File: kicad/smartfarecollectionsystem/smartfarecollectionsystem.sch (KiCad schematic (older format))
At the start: 3 parts

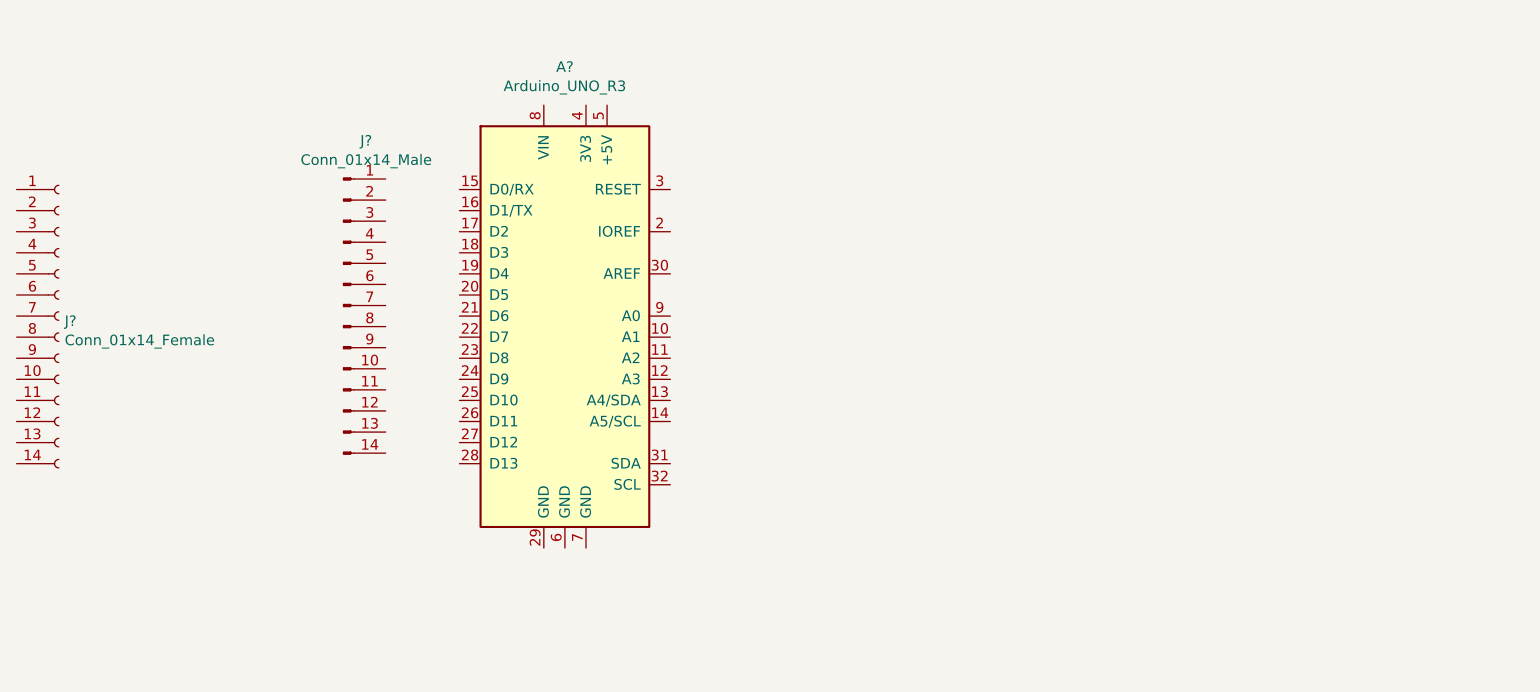
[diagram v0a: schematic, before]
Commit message: ip address changed and PCB layout made
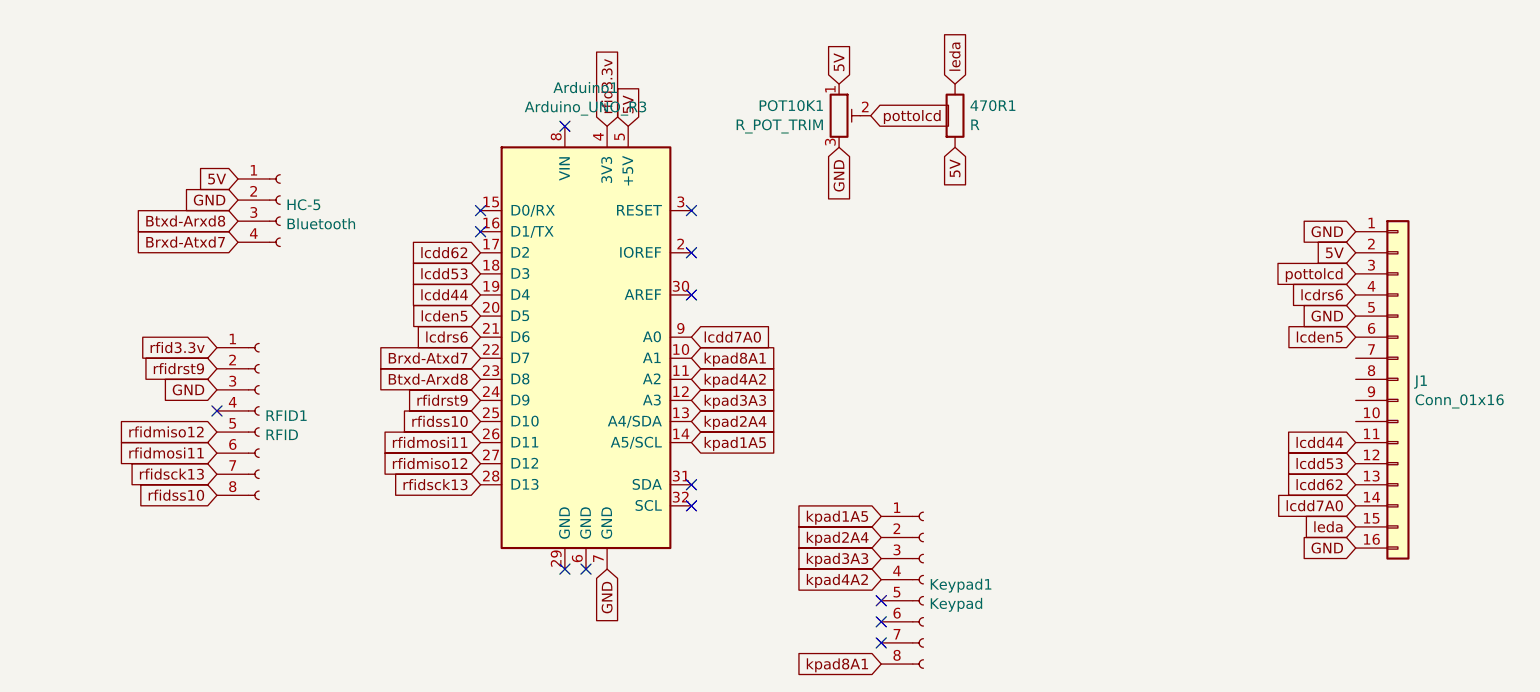
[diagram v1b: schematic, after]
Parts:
- removed J?: Conn_01x14_Female, symbol Connector:Conn_01x14_Female
- removed J?: Conn_01x14_Male, symbol Connector:Conn_01x14_Male
- added 470R1: R, Resistor_THT:R_Axial_DIN0207_L6.3mm_D2.5mm_P7.62mm_Horizontal, symbol Device:R
- added HC-5: Bluetooth, Connector_PinHeader_2.54mm:PinHeader_1x04_P2.54mm_Vertical, symbol Connector:Conn_01x04_Female
- added J1: Conn_01x16, Display:WC1602A, symbol Connector_Generic:Conn_01x16
- added Keypad1: Keypad, Connector_PinHeader_2.54mm:PinHeader_1x08_P2.54mm_Vertical, symbol Connector:Conn_01x08_Female
- added POT10K1: R_POT_TRIM, Potentiometer_THT:Potentiometer_Piher_PT-10-V05_Vertical, symbol Device:R_POT_TRIM
- added RFID1: RFID, Connector_PinHeader_2.54mm:PinHeader_1x08_P2.54mm_Vertical, symbol Connector:Conn_01x08_Female
- gave numbers to parts that had none: 1
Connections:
- net kpad8A1: now reaches Arduino1.10 (A1)
- net kpad8A1: now also Keypad1.8 (Pin_8)
- net kpad4A2: now reaches Arduino1.11 (A2)
- net kpad4A2: now also Keypad1.4 (Pin_4)
- net kpad3A3: now reaches Arduino1.12 (A3)
- net kpad3A3: now also Keypad1.3 (Pin_3)
- net kpad2A4: now reaches Arduino1.13 (A4/SDA)
- net kpad2A4: now also Keypad1.2 (Pin_2)
- net kpad1A5: now reaches Arduino1.14 (A5/SCL)
- net kpad1A5: now also Keypad1.1 (Pin_1)
- net lcdd62: now reaches Arduino1.17 (D2)
- net lcdd62: now also J1.13 (Pin_13)
- net lcdd53: now reaches Arduino1.18 (D3)
- net lcdd53: now also J1.12 (Pin_12)
- net lcdd44: now reaches Arduino1.19 (D4)
- net lcdd44: now also J1.11 (Pin_11)
- net lcden5: now reaches Arduino1.20 (D5)
- net lcden5: now also J1.6 (Pin_6)
- net lcdrs6: now reaches Arduino1.21 (D6)
- net lcdrs6: now also J1.4 (Pin_4)
- net Brxd-Atxd7: now reaches Arduino1.22 (D7)
- net Brxd-Atxd7: now also HC-5.4 (Pin_4)
- net Btxd-Arxd8: now reaches Arduino1.23 (D8)
- net Btxd-Arxd8: now also HC-5.3 (Pin_3)
- net rfidrst9: now reaches Arduino1.24 (D9)
- net rfidrst9: now also RFID1.2 (Pin_2)
- net rfidss10: now reaches Arduino1.25 (D10)
- net rfidss10: now also RFID1.8 (Pin_8)
- net rfidmosi11: now reaches Arduino1.26 (D11)
- net rfidmosi11: now also RFID1.6 (Pin_6)
- net rfidmiso12: now reaches Arduino1.27 (D12)
- net rfidmiso12: now also RFID1.5 (Pin_5)
- net rfidsck13: now reaches Arduino1.28 (D13)
- net rfidsck13: now also RFID1.7 (Pin_7)
- net rfid3.3v: now reaches Arduino1.4 (3V3)
- net rfid3.3v: now also RFID1.1 (Pin_1)
- net 5V: now reaches Arduino1.5 (+5V)
- net 5V: now also 470R1.2, HC-5.1 (Pin_1), J1.2 (Pin_2), POT10K1.1
- net GND: now reaches Arduino1.7 (GND)
- net GND: now also HC-5.2 (Pin_2), J1.1 (Pin_1), J1.16 (Pin_16), J1.5 (Pin_5), POT10K1.3, RFID1.3 (Pin_3)
- net lcdd7A0: now reaches Arduino1.9 (A0)
- net lcdd7A0: now also J1.14 (Pin_14)
- new net leda: 470R1.1, J1.15 (Pin_15)
- new net pottolcd: J1.3 (Pin_3), POT10K1.2
- no-connect marks 0 -> 14
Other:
- moved on the sheet: Arduino1
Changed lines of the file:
@@
 EESchema Schematic File Version 4
+LIBS:smartfarecollectionsystem-cache
 EELAYER 29 0
 EELAYER END
@@
 $EndDescr
 $Comp
-L MCU_Module:Arduino_UNO_R3 A?
+L MCU_Module:Arduino_UNO_R3 Arduino1
 U 1 1 5D211B2A
-P 3450 3300
-F 0 "A?" H 3450 4481 50  0000 C CNN
-F 1 "Arduino_UNO_R3" H 3450 4390 50  0000 C CNN
-F 2 "Module:Arduino_UNO_R3" H 3600 2250 50  0001 L CNN
-F 3 "https://www.arduino.cc/en/Main/arduinoBoardUno" H 3250 4350 50  0001 C CNN
-	1    3450 3300
-	1    0    0    -1
-$EndComp
-$Comp
-L Connector:Conn_01x14_Female J?
-U 1 1 5D21D71C
-P 1050 3300
-F 0 "J?" H 1078 3276 50  0000 L CNN
-F 1 "Conn_01x14_Female" H 1078 3185 50  0000 L CNN
-F 2 "" H 1050 3300 50  0001 C CNN
-F 3 "~" H 1050 3300 50  0001 C CNN
-	1    1050 3300
-	1    0    0    -1
-$EndComp
-$Comp
-L Connector:Conn_01x14_Male J?
-U 1 1 5D22092A
-P 2400 3250
-F 0 "J?" H 2508 4031 50  0000 C CNN
-F 1 "Conn_01x14_Male" H 2508 3940 50  0000 C CNN
-F 2 "" H 2400 3250 50  0001 C CNN
-F 3 "~" H 2400 3250 50  0001 C CNN
-	1    2400 3250
-	1    0    0    -1
-$EndComp
+P 3550 3400
+F 0 "Arduino1" H 3550 4581 50  0000 C CNN
+F 1 "Arduino_UNO_R3" H 3550 4490 50  0000 C CNN
+F 2 "Module:Arduino_UNO_R3" H 3700 2350 50  0001 L CNN
+F 3 "https://www.arduino.cc/en/Main/arduinoBoardUno" H 3350 4450 50  0001 C CNN
+	1    3550 3400
+	1    0    0    -1
+$EndComp
+$Comp
+L Connector:Conn_01x08_Female RFID1
+U 1 1 5D23BC41
+P 2000 3750
+F 0 "RFID1" H 2028 3726 50  0000 L CNN
+F 1 "RFID" H 2028 3635 50  0000 L CNN
+F 2 "Connector_PinHeader_2.54mm:PinHeader_1x08_P2.54mm_Vertical" H 2000 3750 50  0001 C CNN
+F 3 "~" H 2000 3750 50  0001 C CNN
+	1    2000 3750
+	1    0    0    -1
+$EndComp
+$Comp
+L Connector:Conn_01x04_Female HC-5
+U 1 1 5D23DD0F
+P 2100 2750
+F 0 "HC-5" H 2128 2726 50  0000 L CNN
+F 1 "Bluetooth" H 2128 2635 50  0000 L CNN
+F 2 "Connector_PinHeader_2.54mm:PinHeader_1x04_P2.54mm_Vertical" H 2100 2750 50  0001 C CNN
+F 3 "~" H 2100 2750 50  0001 C CNN
+	1    2100 2750
+	1    0    0    -1
+$EndComp
+$Comp
+L Connector:Conn_01x08_Female Keypad1
+U 1 1 5D23F66E
+P 5150 4550
+F 0 "Keypad1" H 5178 4526 50  0000 L CNN
+F 1 "Keypad" H 5178 4435 50  0000 L CNN
+F 2 "Connector_PinHeader_2.54mm:PinHeader_1x08_P2.54mm_Vertical" H 5150 4550 50  0001 C CNN
+F 3 "~" H 5150 4550 50  0001 C CNN
+	1    5150 4550
+	1    0    0    -1
+$EndComp
+Text GLabel 4050 3400 2    50   Input ~ 0
+lcdd7A0
+Text GLabel 7200 4100 0    50   Input ~ 0
+lcdd62
+Text GLabel 3050 3000 0    50   Input ~ 0
+lcdd62
+Text GLabel 7200 4000 0    50   Input ~ 0
+lcdd53
+Text GLabel 3050 3100 0    50   Input ~ 0
+lcdd53
+Text GLabel 7200 3900 0    50   Input ~ 0
+lcdd44
+Text GLabel 3050 3200 0    50   Input ~ 0
+lcdd44
+Text GLabel 7200 3400 0    50   Input ~ 0
+lcden5
+Text GLabel 3050 3300 0    50   Input ~ 0
+lcden5
+Text GLabel 7200 4200 0    50   Input ~ 0
+lcdd7A0
+$Comp
+L Device:R_POT_TRIM POT10K1
+U 1 1 5D25548C
+P 4750 2350
+F 0 "POT10K1" H 4680 2396 50  0000 R CNN
+F 1 "R_POT_TRIM" H 4680 2305 50  0000 R CNN
+F 2 "Potentiometer_THT:Potentiometer_Piher_PT-10-V05_Vertical" H 4750 2350 50  0001 C CNN
+F 3 "~" H 4750 2350 50  0001 C CNN
+	1    4750 2350
+	1    0    0    -1
+$EndComp
+Text GLabel 7200 3200 0    50   Input ~ 0
+lcdrs6
+Text GLabel 3050 3400 0    50   Input ~ 0
+lcdrs6
+Text GLabel 3750 2400 1    50   Input ~ 0
+5V
+$Comp
+L Device:R 470R1
+U 1 1 5D2568DF
+P 5300 2350
+F 0 "470R1" H 5370 2396 50  0000 L CNN
+F 1 "R" H 5370 2305 50  0000 L CNN
+F 2 "Resistor_THT:R_Axial_DIN0207_L6.3mm_D2.5mm_P7.62mm_Horizontal" V 5230 2350 50  0001 C CNN
+F 3 "~" H 5300 2350 50  0001 C CNN
+	1    5300 2350
+	1    0    0    -1
+$EndComp
+Text GLabel 5300 2500 3    50   Input ~ 0
+5V
+Text GLabel 5300 2200 1    50   Input ~ 0
+leda
+Text GLabel 7200 4300 0    50   Input ~ 0
+leda
+Text GLabel 7200 4400 0    50   Input ~ 0
+GND
+Text GLabel 3650 4500 3    50   Input ~ 0
+GND
+Text GLabel 7200 3300 0    50   Input ~ 0
+GND
+Text GLabel 7200 3000 0    50   Input ~ 0
+5V
+Text GLabel 7200 3100 0    50   Input ~ 0
+pottolcd
+Text GLabel 4900 2350 2    50   Input ~ 0
+pottolcd
+Text GLabel 1800 3450 0    50   Input ~ 0
+rfid3.3v
+Text GLabel 3650 2400 1    50   Input ~ 0
+rfid3.3v
+Text GLabel 1800 3550 0    50   Input ~ 0
+rfidrst9
+Text GLabel 3050 3700 0    50   Input ~ 0
+rfidrst9
+Text GLabel 1800 3650 0    50   Input ~ 0
+GND
+NoConn ~ 1800 3750
+Text GLabel 1800 3850 0    50   Input ~ 0
+rfidmiso12
+Text GLabel 3050 4000 0    50   Input ~ 0
+rfidmiso12
+Text GLabel 3050 3900 0    50   Input ~ 0
+rfidmosi11
+Text GLabel 1800 3950 0    50   Input ~ 0
+rfidmosi11
+Text GLabel 1800 4050 0    50   Input ~ 0
+rfidsck13
+Text GLabel 3050 4100 0    50   Input ~ 0
+rfidsck13
+Text GLabel 1800 4150 0    50   Input ~ 0
+rfidss10
+Text GLabel 3050 3800 0    50   Input ~ 0
+rfidss10
+Text GLabel 1900 2650 0    50   Input ~ 0
+5V
+Text GLabel 1900 2750 0    50   Input ~ 0
+GND
+Text GLabel 1900 2850 0    50   Input ~ 0
+Btxd-Arxd8
+Text GLabel 1900 2950 0    50   Input ~ 0
+Brxd-Atxd7
+Text GLabel 3050 3600 0    50   Input ~ 0
+Btxd-Arxd8
+Text GLabel 3050 3500 0    50   Input ~ 0
+Brxd-Atxd7
+NoConn ~ 3450 2400
+NoConn ~ 3050 2800
+NoConn ~ 3050 2900
+NoConn ~ 4050 2800
+NoConn ~ 4050 3000
+NoConn ~ 4050 3200
+Text GLabel 4950 4250 0    50   Input ~ 0
+kpad1A5
+Text GLabel 4050 3900 2    50   Input ~ 0
+kpad1A5
+Text GLabel 4950 4350 0    50   Input ~ 0
+kpad2A4
+Text GLabel 4050 3800 2    50   Input ~ 0
+kpad2A4
+Text GLabel 4950 4450 0    50   Input ~ 0
+kpad3A3
+Text GLabel 4050 3700 2    50   Input ~ 0
+kpad3A3
+Text GLabel 4950 4550 0    50   Input ~ 0
+kpad4A2
+Text GLabel 4050 3600 2    50   Input ~ 0
+kpad4A2
+Text GLabel 4950 4950 0    50   Input ~ 0
+kpad8A1
+Text GLabel 4050 3500 2    50   Input ~ 0
+kpad8A1
+NoConn ~ 4950 4650
+NoConn ~ 4950 4750
+NoConn ~ 4950 4850
+NoConn ~ 4050 4100
+NoConn ~ 4050 4200
+NoConn ~ 3450 4500
+NoConn ~ 3550 4500
+Text GLabel 4750 2200 1    50   Input ~ 0
+5V
+Text GLabel 4750 2500 3    50   Input ~ 0
+GND
+$Comp
+L Connector_Generic:Conn_01x16 J1
+U 1 1 5D288912
+P 7400 3600
+F 0 "J1" H 7480 3592 50  0000 L CNN
+F 1 "Conn_01x16" H 7480 3501 50  0000 L CNN
+F 2 "Display:WC1602A" H 7400 3600 50  0001 C CNN
+F 3 "~" H 7400 3600 50  0001 C CNN
+	1    7400 3600
+	1    0    0    -1
+$EndComp
+Text GLabel 7200 2900 0    50   Input ~ 0
+GND
 $EndSCHEMATC
